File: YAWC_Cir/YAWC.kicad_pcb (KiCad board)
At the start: 2 copper layers, 76 x 38 mm, 16 parts, among them P1 JST-PH_2, P3 CONN_5, P4 CONN_5, P5 CONN_6, U1 TPS769XX, U2 SAMD20J18A-M

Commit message: Update pad sizes
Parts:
- added J_Midi1: CONN_2, Pin_Header_Angled_1x02, F.Cu at (162.6, 114.0)
- added J_Rst1: CONN_2, Pin_Header_Angled_1x02, F.Cu at (179.8, 84.6)
- added R2: 4k7, Resistors_SMD:Resistor_SMD0805_HandSoldering, F.Cu at (176.8, 93.4)
- added R3: 4k7, Resistors_SMD:Resistor_SMD0805_HandSoldering, F.Cu at (189.8, 93.2)
- added R4: R, Resistors_SMD:Resistor_SMD0805_HandSoldering, F.Cu at (150.8, 112.6)
- added SER1: CONN_3X2, Pin_Header_Angled_2x03, F.Cu at (179.6, 103.2)
- added U3: MMA845Q, SMD:QFN16, F.Cu at (182.8, 92.8)
- C4, C7: moved to B.Cu
- P5: footprint Pin_Headers:Pin_Header_Angled_1x06 -> Pin_Header_Angled_1x06
- SWD1: footprint Pin_Headers:Pin_Header_Angled_1x05 -> Pin_Header_Angled_1x05
- moved R1 44.9 mm to (149.8, 89.8), turned to 180 degrees
- moved C7 42.6 mm to (149.6, 96.8), turned to 180 degrees
- moved C4 41.3 mm to (145.6, 100.0), turned to 270 degrees
- moved SWD1 34.1 mm to (162.6, 103.2), turned to 270 degrees
- moved C6 34.1 mm to (147.4, 109.8), turned to 180 degrees
- moved C3 29.4 mm to (157.4, 105.6)
- moved P5 6.00 mm to (162.8, 88.4)
- moved Amp1 0.20 mm to (127.6, 86.0)
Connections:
- C4 pad 1: Net-(C4-Pad1) -> VCC
- C7 pad 2: Net-(C7-Pad2) -> GND
- U2 pad 29: Net-(U2-Pad29) -> /Micro/Tx
- U2 pad 35: Net-(U2-Pad35) -> /Micro/S1P0
- U2 pad 36: Net-(U2-Pad36) -> /Micro/S1P1
- U2 pad 37: Net-(U2-Pad37) -> /Micro/S1P2
- U2 pad 38: Net-(U2-Pad38) -> /Micro/S1P3
- U2 pad 43: Net-(U2-Pad43) -> SDA
- U2 pad 44: Net-(U2-Pad44) -> SCL

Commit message: Buttons. Need to DRC
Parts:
- added P2: Btns, Pin_Headers:Pin_Header_Straight_2x03, F.Cu at (141.4, 114.4)
- C4, C5, C7: moved to F.Cu
- J_Midi1, J_Rst1: footprint Pin_Header_Angled_1x02 -> Pin_Headers:Pin_Header_Angled_1x02
- P5: footprint Pin_Header_Angled_1x06 -> Pin_Headers:Pin_Header_Angled_1x06
- SER1: footprint Pin_Header_Angled_2x03 -> Pin_Headers:Pin_Header_Angled_2x03
- SWD1: footprint Pin_Header_Angled_1x05 -> Pin_Headers:Pin_Header_Straight_1x05
- moved C4 16.1 mm to (129.8, 97.0), turned to 90 degrees
- moved U2 7.42 mm to (141.2, 101.0)
- moved C7 6.51 mm to (145.2, 92.0)
- moved P3 5.60 mm to (125.6, 105.0)
- moved C5 4.64 mm to (152.8, 104.0)
- moved P4 0.20 mm to (130.0, 110.8)
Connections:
- P3 pad 1: /Micro/Y4 -> /Micro/Y14
- P3 pad 2: /Micro/Y2 -> /Micro/Y13
- P3 pad 3: /Micro/Y14 -> /Micro/Y12
- P3 pad 4: /Micro/Y12 -> /Micro/Y11
- P4 pad 1: /Micro/Y11 -> /Micro/Y15
- P4 pad 2: /Micro/Y13 -> /Micro/Y2
- P4 pad 3: /Micro/Y15 -> /Micro/Y3
- P4 pad 4: /Micro/Y3 -> /Micro/Y4
- U2 pad 24: Net-(U2-Pad24) -> /Micro/PB11
- U2 pad 25: Net-(U2-Pad25) -> /Micro/PB12
- U2 pad 26: Net-(U2-Pad26) -> /Micro/PB13
- U2 pad 27: Net-(U2-Pad27) -> /Micro/PB14
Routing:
- net /Micro/Y2: track 21.3 -> 7.78 mm
- net /Micro/Y4: track 21.9 -> 11.1 mm
- net /Micro/Y10: track 19.8 -> 10.0 mm
- net /Micro/Y15: track 16.3 -> 6.56 mm
- net /Micro/Y12: track 20.0 -> 11.3 mm
- net /Micro/Y3: track 17.0 -> 9.75 mm
- net /Micro/Y14: track 20.6 -> 14.7 mm
- net /Micro/Y11: track 16.0 -> 10.9 mm
- net GND: track 18.9 -> 14.9 mm, vias 1 -> 0
- net VCC: track 6.59 -> 3.31 mm, vias 1 -> 0
- net /Micro/Y13: track 15.6 -> 12.3 mm
- net /Micro/Y5: track 17.7 -> 14.9 mm

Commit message: Pin header library
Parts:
- J_Midi1, J_Rst1: footprint Pin_Headers:Pin_Header_Angled_1x02 -> PIN_Hrd:Pin_Header_Angled_1x02
- P2: footprint Pin_Headers:Pin_Header_Straight_2x03 -> PIN_Hrd:Pin_Header_Straight_2x03
- P3, P4: footprint Pin_Headers:Pin_Header_Angled_1x05 -> PIN_Hrd:Pin_Header_Angled_1x05
- P5: footprint Pin_Headers:Pin_Header_Angled_1x06 -> PIN_Hrd:Pin_Header_Angled_1x06
- SER1: footprint Pin_Headers:Pin_Header_Angled_2x03 -> PIN_Hrd:Pin_Header_Angled_2x03
- SWD1: footprint Pin_Headers:Pin_Header_Straight_1x05 -> PIN_Hrd:Pin_Header_Straight_1x05
- moved Amp1 2.27 mm to (128.6, 88.0)
- moved P5 1.28 mm to (163.6, 89.4)
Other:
- board size 76 x 38 mm -> 76 x 36.2 mm

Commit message: More updates. Foot prints still to check
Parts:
- added ATP1: CONN_1, PIN_Hrd:Pin_Header_Straight_1x01, F.Cu at (137.4, 112.4)
- added ATP2: CONN_1, PIN_Hrd:Pin_Header_Straight_1x01, F.Cu at (137.6, 116.0)
- added D1: LED, Diodes_SMD:Diode-SMA_Handsoldering, F.Cu at (139.4, 89.0)
- added R5: 350, CAP_SMD:c_0805, F.Cu at (134.6, 86.0)
- moved P2 2.34 mm to (143.6, 113.6), turned to 90 degrees
- moved C6 1.17 mm to (148.4, 109.2)
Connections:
- P2 pad 2: /Micro/PB12 -> /Micro/PB11
- P2 pad 3: /Micro/PB11 -> /Micro/PB12
- U1 pad 4: Net-(U1-Pad4) -> (no net)
- U2 pad 1: Net-(U2-Pad1) -> (no net)
- U2 pad 2: Net-(U2-Pad2) -> (no net)
- U2 pad 23: Net-(U2-Pad23) -> (no net)
- U2 pad 28: Net-(U2-Pad28) -> (no net)
- U2 pad 30: Net-(U2-Pad30) -> (no net)
- U2 pad 31: Net-(U2-Pad31) -> (no net)
- U2 pad 32: Net-(U2-Pad32) -> (no net)
- U2 pad 39: Net-(U2-Pad39) -> (no net)
- U2 pad 40: Net-(U2-Pad40) -> (no net)
- U2 pad 41: Net-(U2-Pad41) -> (no net)
- U2 pad 42: Net-(U2-Pad42) -> (no net)
- U2 pad 45: Net-(U2-Pad45) -> (no net)
- U2 pad 46: Net-(U2-Pad46) -> (no net)
- U2 pad 49: Net-(U2-Pad49) -> (no net)
- U2 pad 50: Net-(U2-Pad50) -> (no net)
- U2 pad 51: Net-(U2-Pad51) -> (no net)
- U2 pad 53: Net-(U2-Pad53) -> (no net)
- U2 pad 60: Net-(U2-Pad60) -> (no net)
- U3 pad 11: Net-(U3-Pad11) -> (no net)
- U3 pad 13: Net-(U3-Pad13) -> (no net)
- U3 pad 15: Net-(U3-Pad15) -> (no net)
- U3 pad 16: Net-(U3-Pad16) -> (no net)
- U3 pad 2: Net-(U3-Pad2) -> (no net)
- U3 pad 3: Net-(U3-Pad3) -> (no net)
- U3 pad 8: Net-(U3-Pad8) -> (no net)
- U3 pad 9: Net-(U3-Pad9) -> (no net)

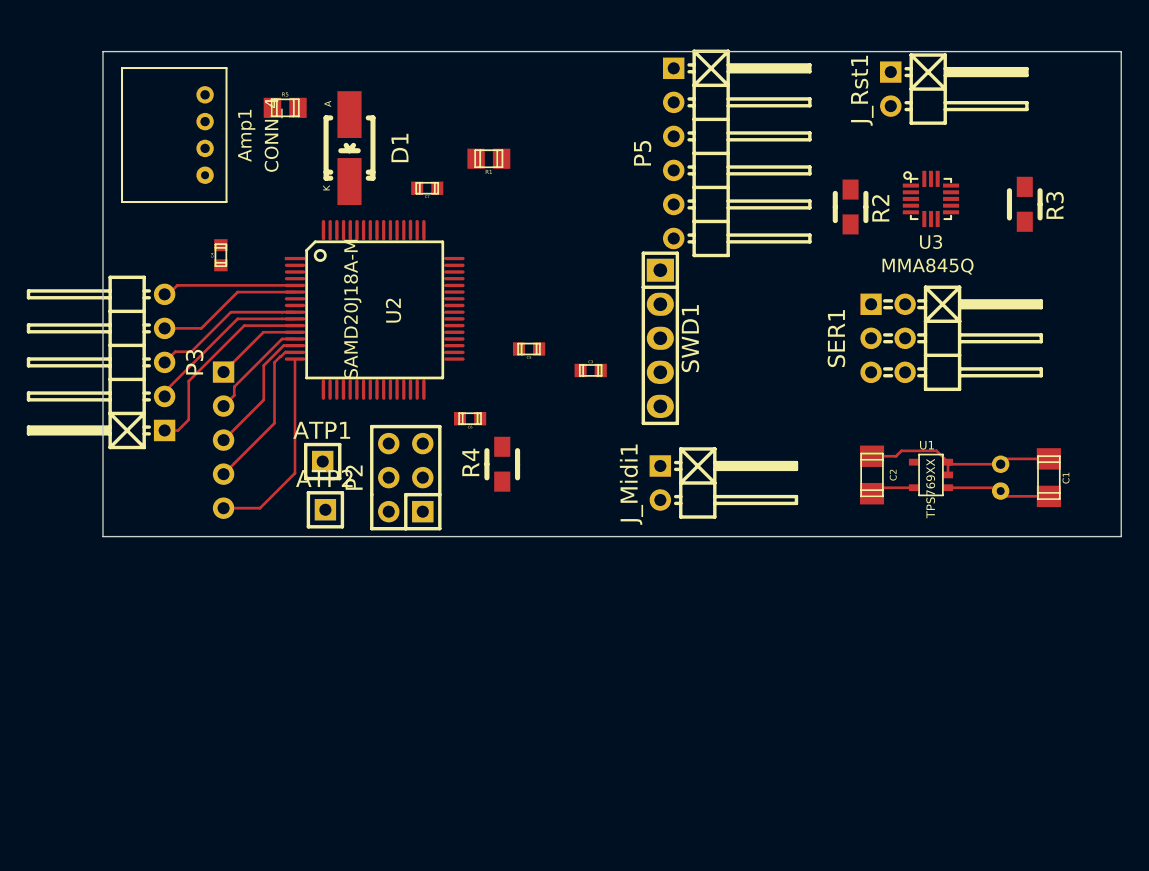
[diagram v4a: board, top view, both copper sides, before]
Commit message: Route not finished. Components done
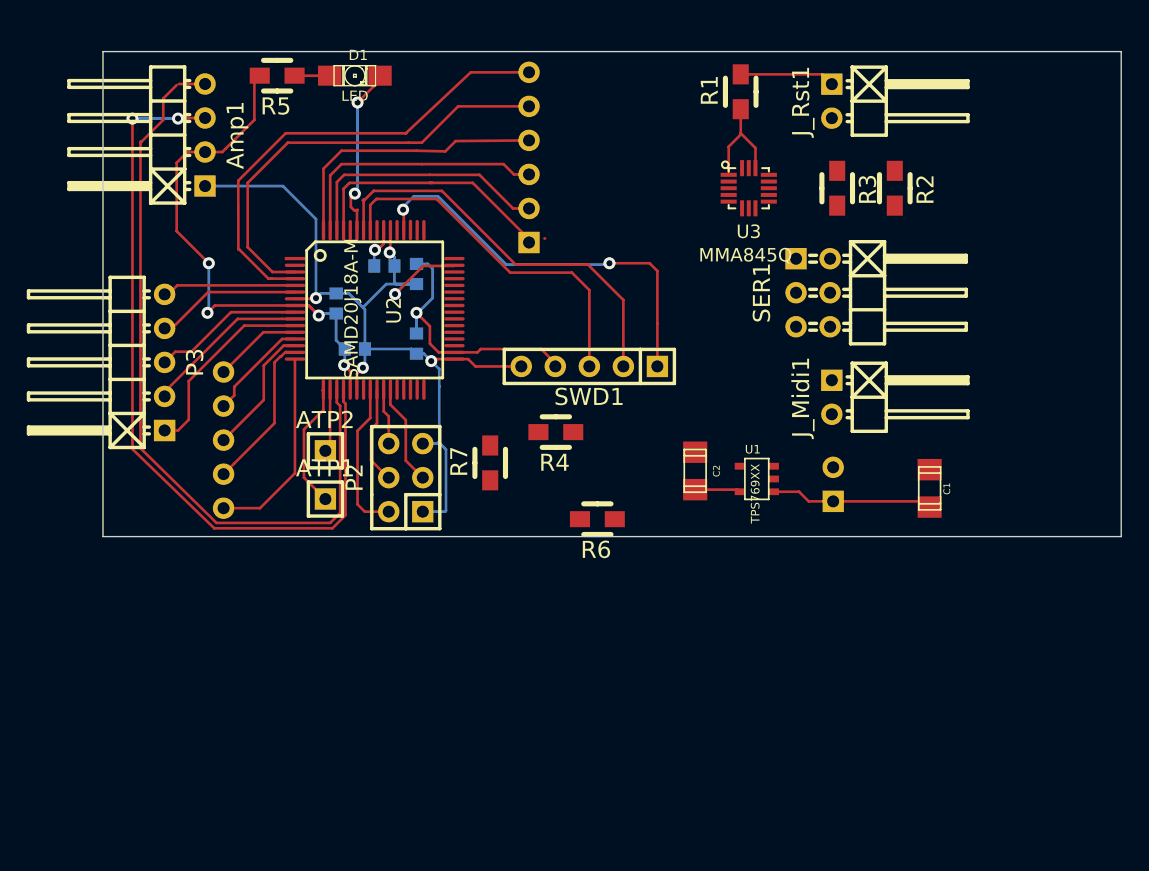
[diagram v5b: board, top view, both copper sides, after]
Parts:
- added R6: 4k, Resistors_SMD:Resistor_SMD0805_HandSoldering, F.Cu at (157.9, 116.7)
- added R7: 1k, Resistors_SMD:Resistor_SMD0805_HandSoldering, F.Cu at (149.9, 112.5)
- Amp1: footprint JST:JST-4-PH-RA -> PIN_Hdr:Pin_Header_Angled_1x04
- C3, C4, C5, C6, C7, P5: moved to B.Cu
- D1: footprint Diodes_SMD:Diode-SMA_Handsoldering -> SMD:LED-1206
- P1: footprint JST:JST-2-PH-RA -> PIN_Hdr:Pin_Header_Angled_1x02
- R1: footprint Capacitors_SMD:c_0805 -> Resistors_SMD:Resistor_SMD0805_HandSoldering
- R5: footprint CAP_SMD:c_0805 -> Resistors_SMD:Resistor_SMD0805_HandSoldering
- SWD1: footprint PIN_Hrd:Pin_Header_Straight_1x05 -> PIN_Hdr:Pin_Header_Straight_1x05
- moved R1 19.5 mm to (168.6, 84.8), turned to 90 degrees
- moved J_Midi1 14.3 mm to (175.4, 107.6)
- moved R3 14.1 mm to (175.8, 92.0)
- moved U3 13.6 mm to (169.2, 92.0)
- moved C2 13.2 mm to (165.2, 113.1)
- moved C3 13.2 mm to (144.4, 103.6), turned to 90 degrees
- moved U1 13.0 mm to (169.8, 113.7)
- moved P1 12.5 mm to (175.5, 114.1)
- moved P5 10.8 mm to (152.8, 89.7), turned to 90 degrees
- moved C5 10.1 mm to (144.4, 98.4), turned to 90 degrees
- moved C6 10.0 mm to (139.8, 104.0)
- moved C4 9.32 mm to (138.4, 100.6), turned to 270 degrees
- moved C1 8.94 mm to (182.7, 114.4)
- moved C7 6.62 mm to (142.0, 97.8)
- moved SER1 6.55 mm to (174.0, 99.8)
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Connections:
- net Net-(ATP2-Pad1) renamed BatSample
- P2 pad 3: /Micro/PB12 -> /Micro/PB14
- P2 pad 4: /Micro/PB13 -> /Micro/PB12
- P2 pad 6: /Micro/PB14 -> /Micro/PB13
- P5 pad 1: /Micro/Y0 -> /Micro/Y6
- P5 pad 2: /Micro/Y1 -> /Micro/Y7
- P5 pad 3: /Micro/Y9 -> /Micro/Y8
- P5 pad 4: /Micro/Y8 -> /Micro/Y9
- P5 pad 5: /Micro/Y7 -> /Micro/Y0
- P5 pad 6: /Micro/Y6 -> /Micro/Y1
- U1 pad 4: (no net) -> Net-(U1-Pad4)
- U2 pad 1: (no net) -> Net-(U2-Pad1)
- U2 pad 2: (no net) -> Net-(U2-Pad2)
- U2 pad 23: (no net) -> Net-(U2-Pad23)
- U2 pad 28: (no net) -> Net-(U2-Pad28)
- U2 pad 30: (no net) -> Net-(U2-Pad30)
- U2 pad 31: (no net) -> Net-(U2-Pad31)
- U2 pad 32: (no net) -> Net-(U2-Pad32)
- U2 pad 39: (no net) -> Net-(U2-Pad39)
- U2 pad 40: (no net) -> Net-(U2-Pad40)
- U2 pad 41: (no net) -> Net-(U2-Pad41)
- U2 pad 42: (no net) -> Net-(U2-Pad42)
- U2 pad 45: (no net) -> Net-(U2-Pad45)
- U2 pad 46: (no net) -> Net-(U2-Pad46)
- U2 pad 49: (no net) -> Net-(U2-Pad49)
- U2 pad 50: (no net) -> Net-(U2-Pad50)
- U2 pad 51: (no net) -> Net-(U2-Pad51)
- U2 pad 53: (no net) -> Net-(U2-Pad53)
- U2 pad 60: (no net) -> Net-(U2-Pad60)
- U3 pad 11: (no net) -> Net-(U3-Pad11)
- U3 pad 13: (no net) -> Net-(U3-Pad13)
- U3 pad 15: (no net) -> Net-(U3-Pad15)
- U3 pad 16: (no net) -> Net-(U3-Pad16)
- U3 pad 2: (no net) -> Net-(U3-Pad2)
- U3 pad 3: (no net) -> Net-(U3-Pad3)
- U3 pad 8: (no net) -> Net-(U3-Pad8)
- U3 pad 9: (no net) -> Net-(U3-Pad9)
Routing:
- net VCC: track 3.31 -> 71.8 mm, vias 0 -> 5
- net Bth: track 0.00 -> 58.3 mm, vias 0 -> 2
- net GND: track 14.9 -> 73.2 mm, vias 0 -> 5
- net Vib: track 0.00 -> 57.0 mm
- net /Micro/Reset: track 0.00 -> 37.7 mm, vias 0 -> 2
- net /Micro/Y1: track 0.00 -> 35.3 mm
- net /Micro/Y0: track 0.00 -> 32.5 mm
- net /Micro/SWDIO: track 0.00 -> 30.4 mm
- net /Micro/SWCLK: track 0.00 -> 26.9 mm
- net /Micro/Y9: track 0.00 -> 20.8 mm
- net /Micro/Y8: track 0.00 -> 19.6 mm
- net /Micro/Y6: track 0.00 -> 19.3 mm
- net /Micro/Y7: track 0.00 -> 19.2 mm
- net Net-(D1-Pad2): track 0.00 -> 12.6 mm, vias 0 -> 2
- net /Micro/PB11: track 0.00 -> 11.5 mm
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
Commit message: More
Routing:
- net VCC: track 71.8 -> 138.7 mm, vias 5 -> 9
- net GND: track 73.2 -> 97.8 mm, vias 5 -> 6
- net /Micro/Reset: track 37.7 -> 60.7 mm, vias 2 -> 4

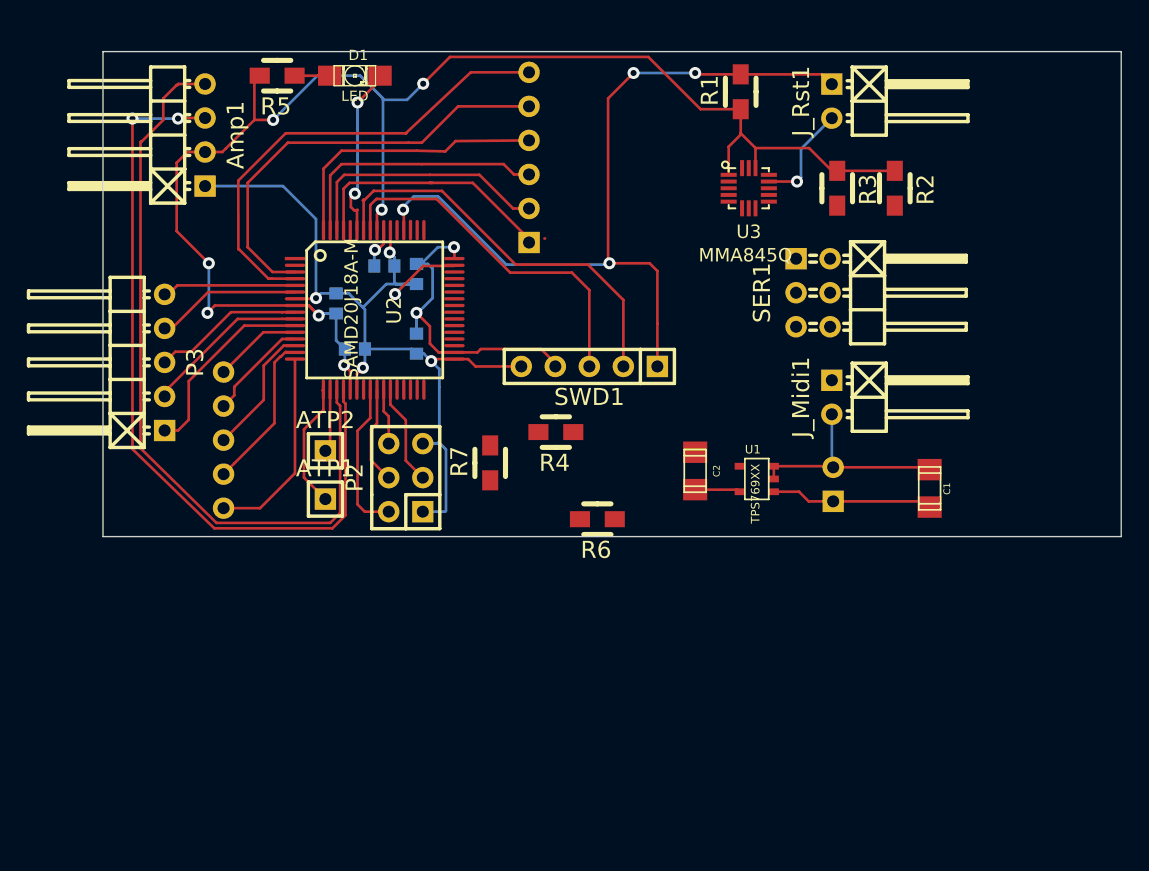
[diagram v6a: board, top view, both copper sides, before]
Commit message: All routed and DRC No gnd fill No silk screen detail done
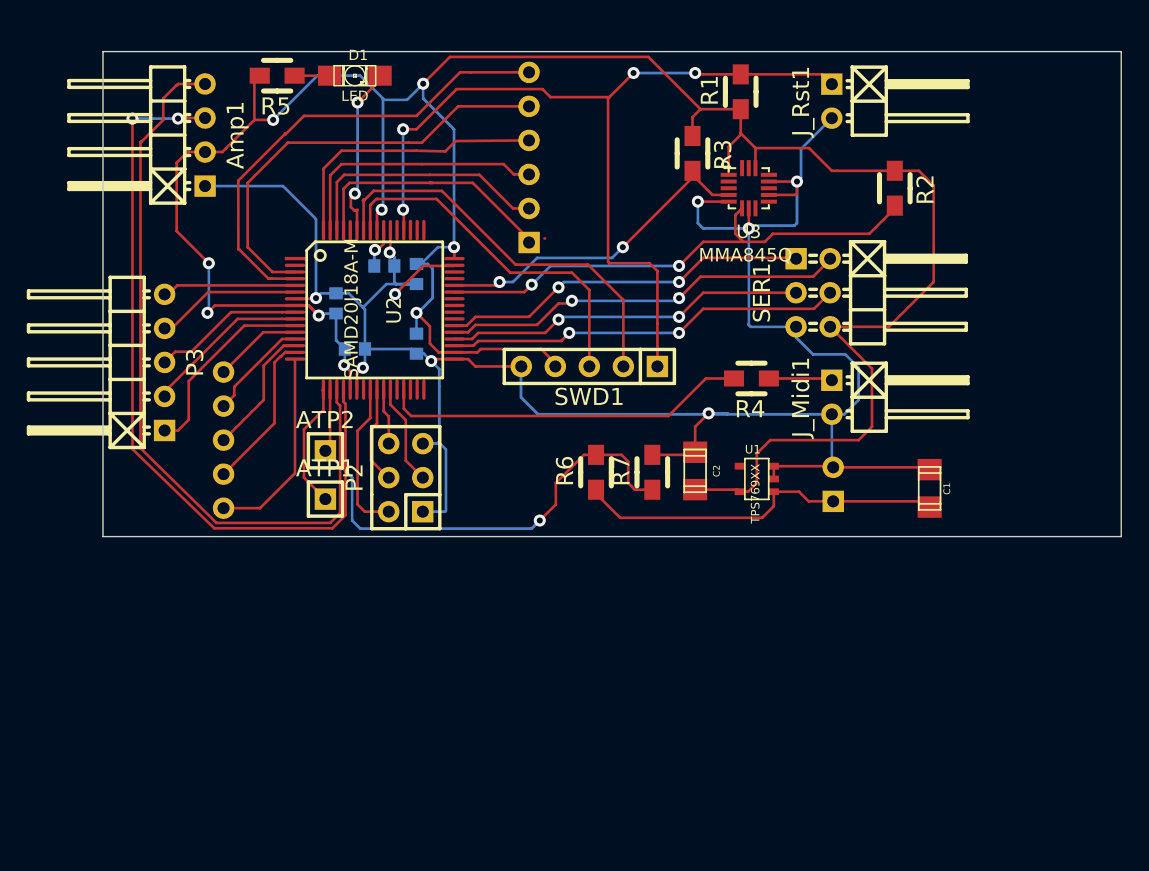
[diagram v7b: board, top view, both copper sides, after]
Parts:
- moved R4 15.1 mm to (169.4, 106.2)
- moved R7 12.1 mm to (162.0, 113.2)
- moved R3 11.1 mm to (165.0, 89.4)
- moved R6 3.50 mm to (157.8, 113.2), turned to 90 degrees
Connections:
- SER1 pad 1: /Micro/S1P0 -> /Micro/S1P3
- SER1 pad 2: /Micro/S1P1 -> /Micro/S1P2
- SER1 pad 3: /Micro/S1P2 -> /Micro/S1P1
- SER1 pad 4: /Micro/S1P3 -> /Micro/S1P0
- U1 pad 4: Net-(U1-Pad4) -> (no net)
- U2 pad 1: Net-(U2-Pad1) -> (no net)
- U2 pad 2: Net-(U2-Pad2) -> (no net)
- U2 pad 23: Net-(U2-Pad23) -> (no net)
- U2 pad 28: Net-(U2-Pad28) -> (no net)
- U2 pad 30: Net-(U2-Pad30) -> (no net)
- U2 pad 31: Net-(U2-Pad31) -> (no net)
- U2 pad 32: Net-(U2-Pad32) -> (no net)
- U2 pad 39: Net-(U2-Pad39) -> (no net)
- U2 pad 40: Net-(U2-Pad40) -> (no net)
- U2 pad 41: Net-(U2-Pad41) -> (no net)
- U2 pad 42: Net-(U2-Pad42) -> (no net)
- U2 pad 45: Net-(U2-Pad45) -> (no net)
- U2 pad 46: Net-(U2-Pad46) -> (no net)
- U2 pad 49: Net-(U2-Pad49) -> (no net)
- U2 pad 50: Net-(U2-Pad50) -> (no net)
- U2 pad 51: Net-(U2-Pad51) -> (no net)
- U2 pad 53: Net-(U2-Pad53) -> (no net)
- U2 pad 60: Net-(U2-Pad60) -> (no net)
- U3 pad 11: Net-(U3-Pad11) -> (no net)
- U3 pad 13: Net-(U3-Pad13) -> (no net)
- U3 pad 15: Net-(U3-Pad15) -> (no net)
- U3 pad 16: Net-(U3-Pad16) -> (no net)
- U3 pad 2: Net-(U3-Pad2) -> (no net)
- U3 pad 3: Net-(U3-Pad3) -> (no net)
- U3 pad 8: Net-(U3-Pad8) -> (no net)
- U3 pad 9: Net-(U3-Pad9) -> (no net)
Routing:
- net GND: track 97.8 -> 173.3 mm, vias 6 -> 9
- net VCC: track 138.7 -> 195.8 mm
- net SDA: track 0.00 -> 38.6 mm, vias 0 -> 2
- net BatSample: track 4.71 -> 38.6 mm, vias 0 -> 1
- net /Micro/S1P2: track 0.00 -> 30.4 mm, vias 0 -> 2
- net /Micro/S1P0: track 0.00 -> 29.7 mm, vias 0 -> 2
- net /Micro/S1P3: track 0.00 -> 27.6 mm, vias 0 -> 2
- net /Micro/Tx: track 0.00 -> 27.5 mm
- net /Micro/S1P1: track 0.00 -> 26.9 mm, vias 0 -> 2
- net SCL: track 0.00 -> 25.2 mm, vias 0 -> 2
- net /Vbatt: track 12.1 -> 27.9 mm
- net /Micro/Reset: track 60.7 -> 65.6 mm
- net Net-(J_Midi1-Pad1): track 0.00 -> 4.75 mm

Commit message: Board resized
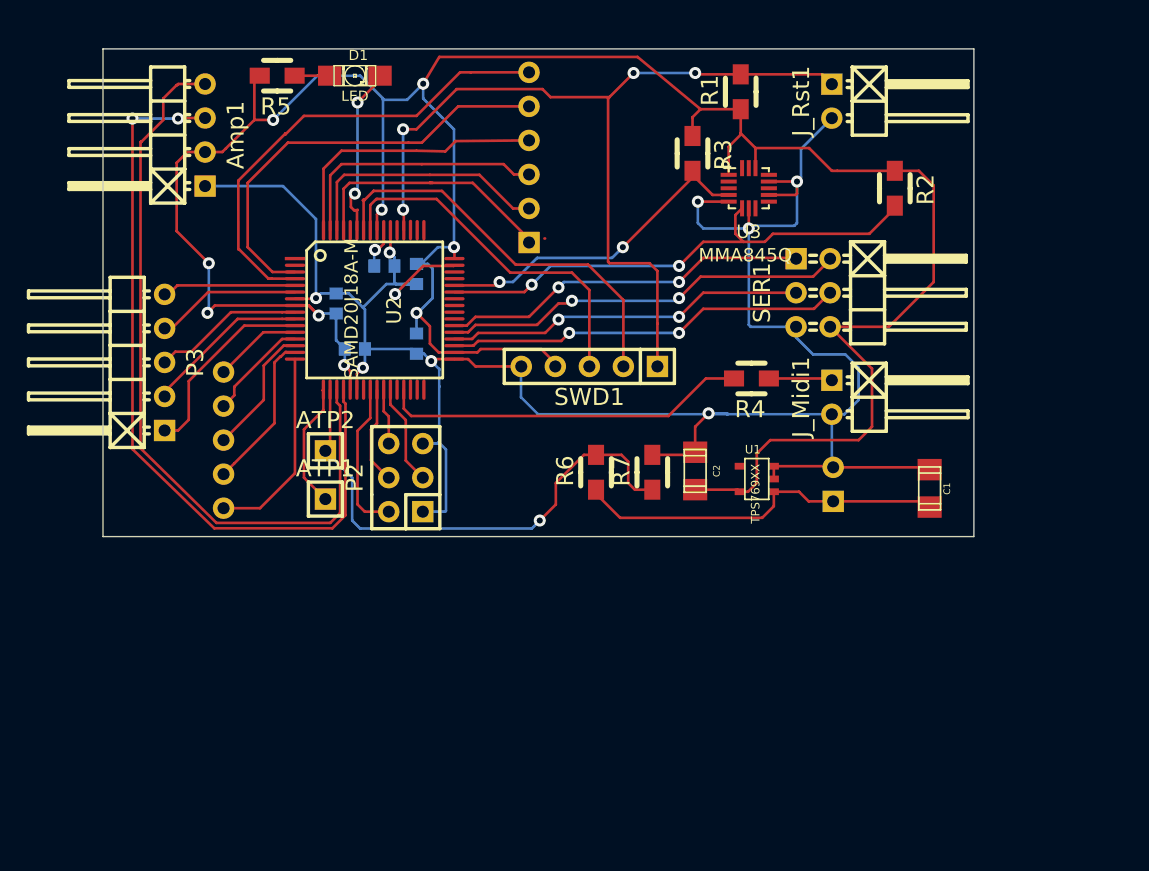
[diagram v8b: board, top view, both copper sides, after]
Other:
- board size 76 x 36.2 mm -> 65 x 36.4 mm
